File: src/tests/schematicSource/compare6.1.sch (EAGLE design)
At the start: 8 parts, among them Q1 BSS92, Q2 BSS92, Q3 BSS97, Q4 BSS97, Q5 BSS92

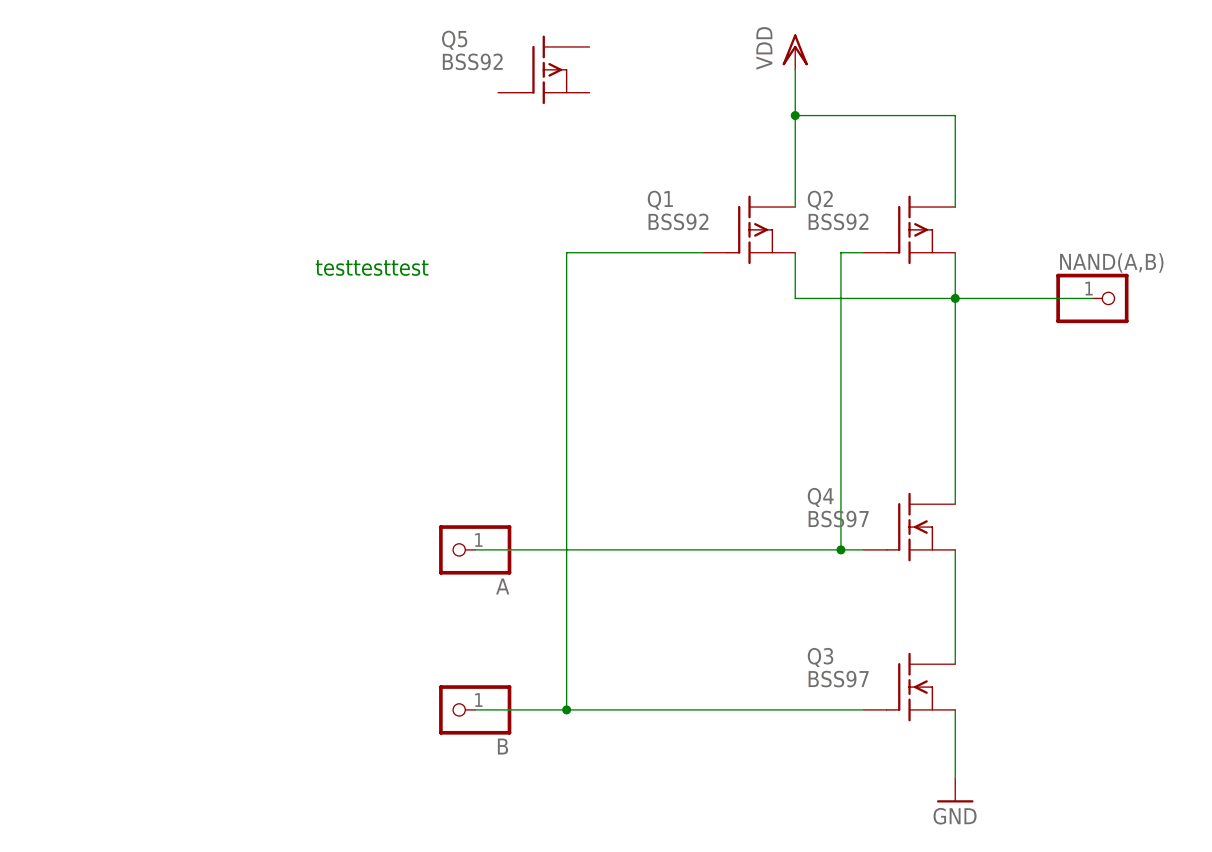
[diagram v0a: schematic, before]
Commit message: added more test cases, including transformation schematic -> eaglemodel -> schematic -> eaglemodel and compared the models, schematic comparison is missing
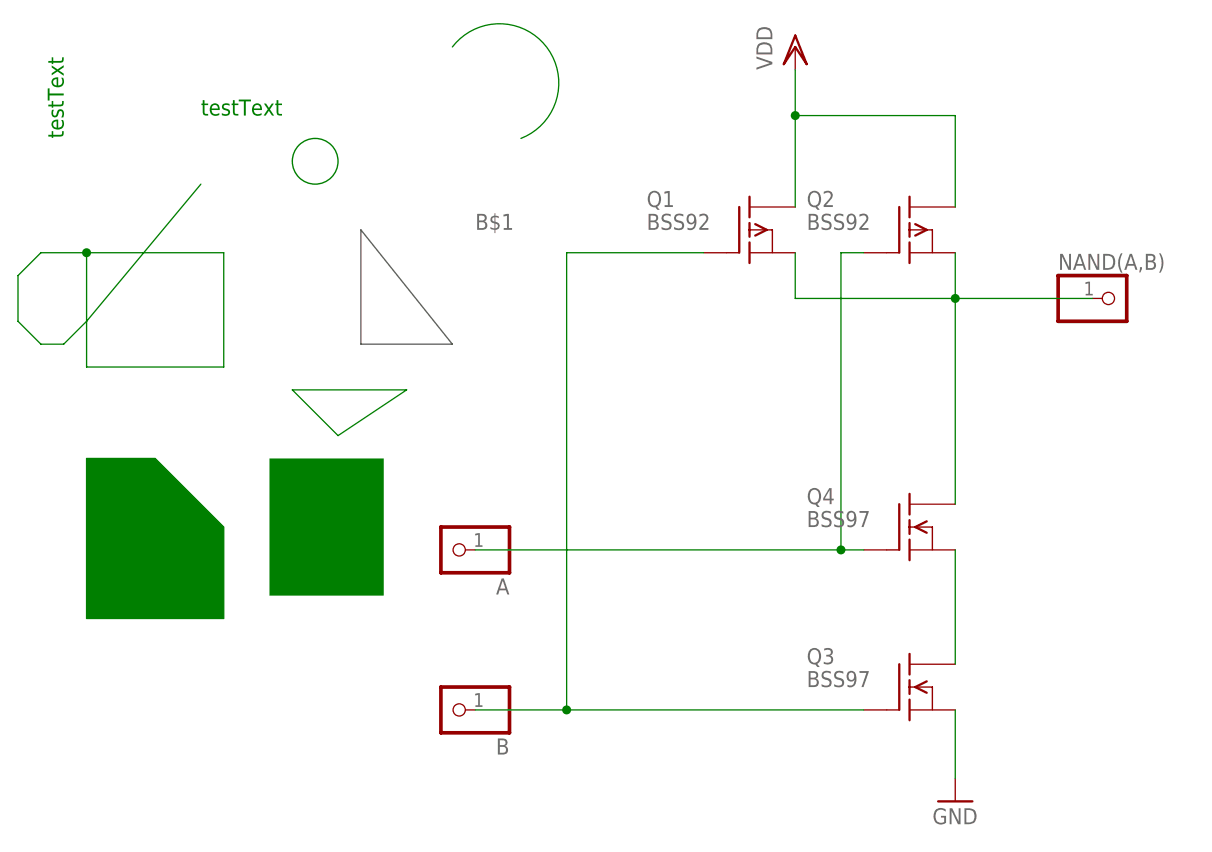
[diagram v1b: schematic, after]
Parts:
- removed Q5: BSS92, transistor-fet:BSS92
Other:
- note added: "testText"
- note removed: "testtesttest"
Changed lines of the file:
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@@
 <part name="A" library="pinhead" deviceset="PINHD-1X1" device=""/>
 <part name="B" library="pinhead" deviceset="PINHD-1X1" device=""/>
-<part name="Q5" library="transistor-fet" deviceset="BSS92" device="">
-<attribute name="P1" value="0001"/>
-<attribute name="TEST2" value="5"/>
-<attribute name="UID" value="8"/>
-</part>
 </parts>
 <sheets>
 <sheet>
 <plain>
-<text x="-231.14" y="167.64" size="1.778" layer="91">testtesttest</text>
+<text x="-243.84" y="185.42" size="1.778" layer="91">testText</text>
+<text x="-259.08" y="182.88" size="1.778" layer="91" rot="R90">testText</text>
+<circle x="-231.14" y="180.34" radius="2.54" width="0.1524" layer="91"/>
+<dimension x1="-232.93605" y1="182.13605" x2="-229.34395" y2="178.54395" x3="-223.519996875" y3="187.96" textsize="1.778" layer="91" dtype="diameter"/>
+<polygon width="0.1524" layer="91">
+<vertex x="-256.54" y="147.32"/>
+<vertex x="-256.54" y="129.54"/>
+<vertex x="-241.3" y="129.54"/>
+<vertex x="-241.3" y="139.7"/>
+<vertex x="-248.92" y="147.32"/>
+</polygon>
+<rectangle x1="-236.22" y1="132.08" x2="-223.52" y2="147.32" layer="91"/>
 </plain>
 <instances>
@@
 <instance part="A" gate="G$1" x="-215.9" y="137.16" rot="R180"/>
 <instance part="B" gate="G$1" x="-215.9" y="119.38" rot="R180"/>
-<instance part="Q5" gate="G$1" x="-205.74" y="190.5">
-<attribute name="P1" x="-205.74" y="190.5" size="1.778" layer="96" display="off"/>
-<attribute name="TEST2" x="-205.74" y="190.5" size="1.778" layer="96" display="off"/>
-<attribute name="UID" x="-205.74" y="190.5" size="1.778" layer="96" display="off"/>
-</instance>
 </instances>
 <busses>
+<bus name="B$1">
+<segment>
+<wire x1="-226.06" y1="172.72" x2="-226.06" y2="160.02" width="0.762" layer="92"/>
+<wire x1="-226.06" y1="160.02" x2="-215.9" y2="160.02" width="0.762" layer="92"/>
+<wire x1="-215.9" y1="160.02" x2="-226.06" y2="172.72" width="0.762" layer="92"/>
+<label x="-213.36" y="172.72" size="1.778" layer="95"/>
+</segment>
+</bus>
 </busses>
 <nets>
@@
 </segment>
 </net>
+<net name="N$1" class="0">
+<segment>
+<wire x1="-256.54" y1="170.18" x2="-241.3" y2="170.18" width="0.1524" layer="91"/>
+<wire x1="-241.3" y1="170.18" x2="-241.3" y2="157.48" width="0.1524" layer="91"/>
+<wire x1="-241.3" y1="157.48" x2="-256.54" y2="157.48" width="0.1524" layer="91"/>
+<wire x1="-256.54" y1="157.48" x2="-256.54" y2="162.56" width="0.1524" layer="91"/>
+<wire x1="-256.54" y1="162.56" x2="-256.54" y2="170.18" width="0.1524" layer="91"/>
+<wire x1="-256.54" y1="170.18" x2="-261.62" y2="170.18" width="0.1524" layer="91"/>
+<wire x1="-261.62" y1="170.18" x2="-264.16" y2="167.64" width="0.1524" layer="91"/>
+<wire x1="-264.16" y1="167.64" x2="-264.16" y2="162.56" width="0.1524" layer="91"/>
+<wire x1="-264.16" y1="162.56" x2="-261.62" y2="160.02" width="0.1524" layer="91"/>
+<wire x1="-261.62" y1="160.02" x2="-259.08" y2="160.02" width="0.1524" layer="91"/>
+<wire x1="-259.08" y1="160.02" x2="-256.54" y2="162.56" width="0.1524" layer="91"/>
+<wire x1="-256.54" y1="162.56" x2="-243.84" y2="177.8" width="0.1524" layer="91"/>
+<junction x="-256.54" y="170.18"/>
+</segment>
+</net>
+<net name="N$3" class="0">
+<segment>
+<wire x1="-233.68" y1="154.94" x2="-220.98" y2="154.94" width="0.1524" layer="91"/>
+<wire x1="-220.98" y1="154.94" x2="-228.6" y2="149.86" width="0.1524" layer="91"/>
+<wire x1="-228.6" y1="149.86" x2="-233.68" y2="154.94" width="0.1524" layer="91"/>
+</segment>
+</net>
+<net name="N$4" class="0">
+<segment>
+<wire x1="-215.9" y1="193.04" x2="-208.28" y2="182.88" width="0.1524" layer="91" curve="-211.328693"/>
+</segment>
+</net>
